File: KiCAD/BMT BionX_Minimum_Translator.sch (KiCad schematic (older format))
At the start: 18 parts

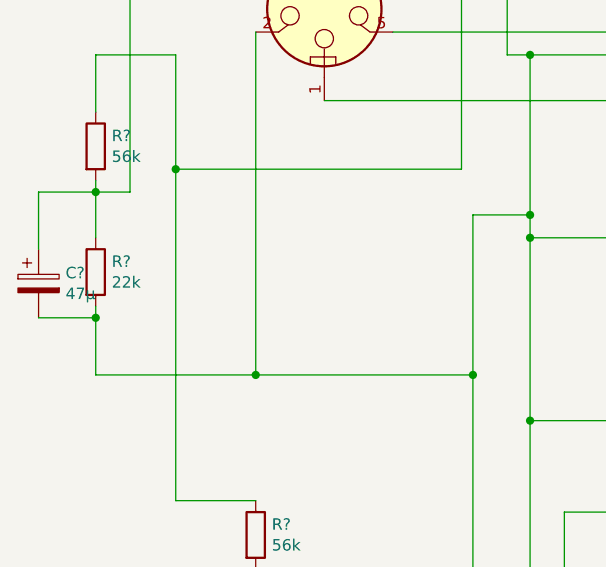
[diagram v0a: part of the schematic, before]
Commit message: Zener diode at HiSide-Switch input added
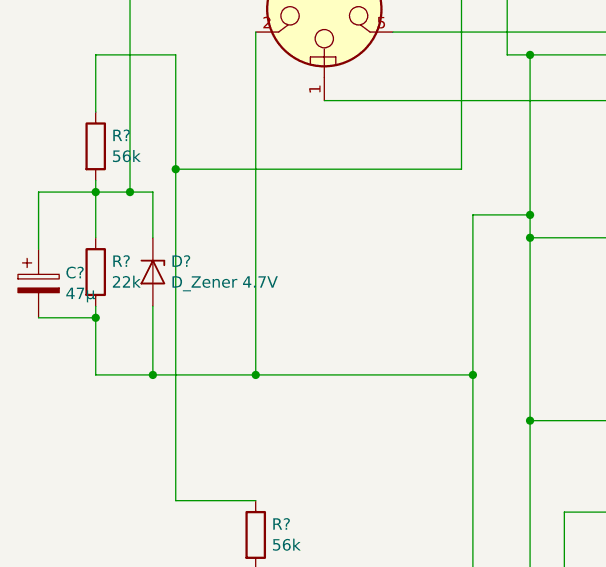
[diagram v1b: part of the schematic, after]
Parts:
- added D?: D_Zener 4.7V, symbol Device:D_Zener
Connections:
- wire segments 150 -> 154
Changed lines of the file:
@@
 	1250 4100 1250 4350
 Wire Wire Line
-	1250 4350 1950 4350
+	1250 4350 1500 4350
 Wire Wire Line
 	2200 2200 2200 1950
@@
 Wire Wire Line
 	3150 2950 4600 2950
+$Comp
+L Device:D_Zener D?
+U 1 1 5F25BD75
+P 1500 3900
+F 0 "D?" V 1454 3979 50  0000 L CNN
+F 1 "D_Zener 4.7V" V 1545 3979 50  0000 L CNN
+F 2 "" H 1500 3900 50  0001 C CNN
+F 3 "~" H 1500 3900 50  0001 C CNN
+	1    1500 3900
+	0    1    1    0
+$EndComp
+Wire Wire Line
+	1400 3550 1500 3550
+Wire Wire Line
+	1500 3550 1500 3750
+Connection ~ 1400 3550
+Wire Wire Line
+	1500 4050 1500 4350
+Connection ~ 1500 4350
+Wire Wire Line
+	1500 4350 1950 4350
 $EndSCHEMATC

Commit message: bugfix in pinout of BTS432
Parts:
- removed U?: BTS432, Package_TO_SOT_SMD:TO-263-7_TabPin4, symbol Power_Management:BTS50010-1TAD
- added U?: BTS432, Package_TO_SOT_SMD:TO-263-7_TabPin4, symbol Power_Management:BTS432
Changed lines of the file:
@@
 	1600 2950 1600 3450
 Connection ~ 1600 3450
-$Comp
-L Power_Management:BTS50010-1TAD U?
-U 1 1 5F329D26
-P 3050 2050
-F 0 "U?" H 3394 2096 50  0000 L CNN
-F 1 "BTS432" H 3394 2005 50  0000 L CNN
-F 2 "Package_TO_SOT_SMD:TO-263-7_TabPin4" H 3900 1750 50  0001 C CNN
-F 3 "https://www.infineon.com/dgdl/Infineon-BTS50010-1TAD-DS-v01_00-EN.pdf?fileId=5546d462576f34750157c38810ca55cd" H 3050 1650 50  0001 C CNN
-	1    3050 2050
-	1    0    0    -1
-$EndComp
 Connection ~ 1950 4350
 Wire Wire Line
@@
 Wire Wire Line
 	1500 4350 1950 4350
+$Comp
+L Power_Management:BTS432 U?
+U 1 1 5F27B110
+P 3050 2050
+F 0 "U?" H 3394 2096 50  0000 L CNN
+F 1 "BTS432" H 3394 2005 50  0000 L CNN
+F 2 "Package_TO_SOT_SMD:TO-263-7_TabPin4" H 3900 1750 50  0001 C CNN
+F 3 "https://www.infineon.com/dgdl/Infineon-BTS50010-1TAD-DS-v01_00-EN.pdf?fileId=5546d462576f34750157c38810ca55cd" H 3050 1650 50  0001 C CNN
+	1    3050 2050
+	1    0    0    -1
+$EndComp
 $EndSCHEMATC

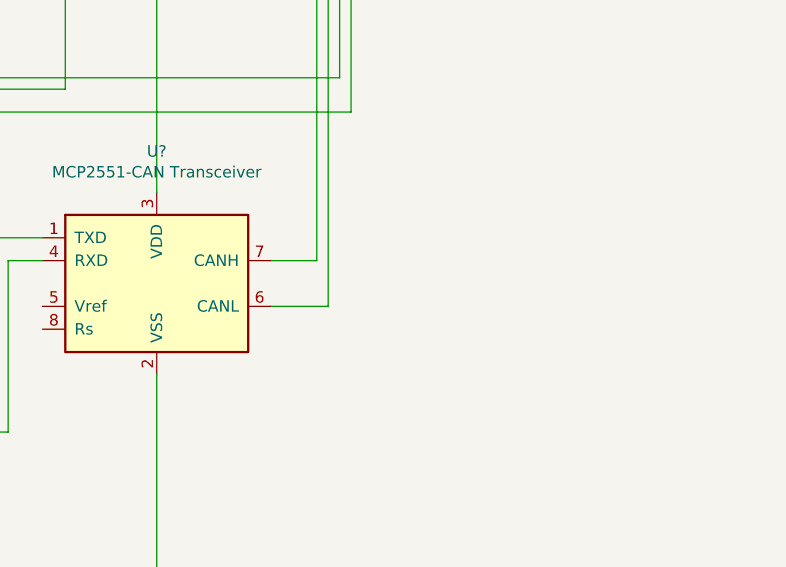
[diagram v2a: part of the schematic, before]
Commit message: Can termination resistor added
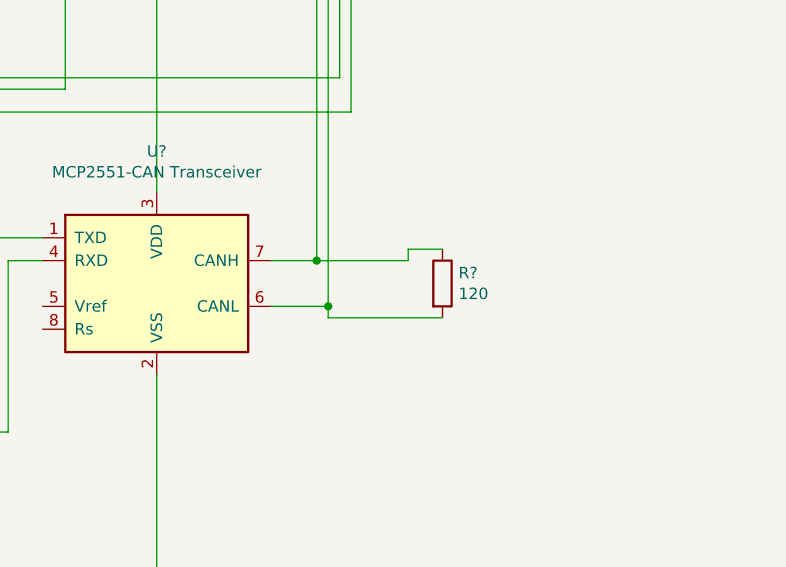
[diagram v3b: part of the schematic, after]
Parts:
- added R?: 120, symbol Device:R
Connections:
- net at J?.3 (Pin_3), U?.7 (CANH): now also R?.1
- net at J?.4 (Pin_4), U?.6 (CANL): now also R?.2
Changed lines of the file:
@@
 	1    0    0    -1
 $EndComp
+$Comp
+L Device:R R?
+U 1 1 5F28C11A
+P 7950 5650
+F 0 "R?" H 8020 5696 50  0000 L CNN
+F 1 "120" H 8020 5605 50  0000 L CNN
+F 2 "" V 7880 5650 50  0001 C CNN
+F 3 "~" H 7950 5650 50  0001 C CNN
+	1    7950 5650
+	1    0    0    -1
+$EndComp
+Wire Wire Line
+	7400 5550 7800 5550
+Wire Wire Line
+	7800 5550 7800 5500
+Wire Wire Line
+	7800 5500 7950 5500
+Connection ~ 7400 5550
+Wire Wire Line
+	7950 5800 7450 5800
+Wire Wire Line
+	7450 5800 7450 5750
+Connection ~ 7450 5750
 $EndSCHEMATC

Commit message: update KiCAD schematic
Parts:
- added J?: CAN Terminator, symbol Connector:Conn_01x02_Female
- added J?: CAN Connector, symbol Connector:Conn_01x02_Male
- added J?: Throttle connector, symbol Connector:Conn_01x03_Female
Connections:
- net at C?.2, D?.2 (A), J?.2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: now also J?.3 (Pin_3)
- net at J?.1 (Pin_1), U?.1 (OUT), U?.3 (VDD)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: now also J?.1 (Pin_1)
- net at J?.3 (Pin_3), U?.7 (CANH): now also J?.1 (Pin_1); no longer R?.1
- net at J?.4 (Pin_4), U?.6 (CANL): now also J?.2 (Pin_2); no longer R?.2
- net at U?.PA3: now also J?.2 (Pin_2)
- new net: J?.1 (Pin_1), R?.1
- new net: J?.2 (Pin_2), R?.2
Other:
- moved on the sheet: R?
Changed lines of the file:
@@
 Connection ~ 6700 2750
 Wire Wire Line
-	6700 2750 7550 2750
+	6700 2750 7300 2750
 Wire Wire Line
 	4850 7550 6700 7550
@@
 L Device:R R?
 U 1 1 5F28C11A
-P 7950 5650
-F 0 "R?" H 8020 5696 50  0000 L CNN
-F 1 "120" H 8020 5605 50  0000 L CNN
-F 2 "" V 7880 5650 50  0001 C CNN
-F 3 "~" H 7950 5650 50  0001 C CNN
-	1    7950 5650
-	1    0    0    -1
-$EndComp
-Wire Wire Line
-	7400 5550 7800 5550
-Wire Wire Line
-	7800 5550 7800 5500
-Wire Wire Line
-	7800 5500 7950 5500
+P 9400 5750
+F 0 "R?" H 9470 5796 50  0000 L CNN
+F 1 "120" H 9470 5705 50  0000 L CNN
+F 2 "" V 9330 5750 50  0001 C CNN
+F 3 "~" H 9400 5750 50  0001 C CNN
+	1    9400 5750
+	1    0    0    -1
+$EndComp
 Connection ~ 7400 5550
-Wire Wire Line
-	7950 5800 7450 5800
 Wire Wire Line
 	7450 5800 7450 5750
 Connection ~ 7450 5750
+$Comp
+L Connector:Conn_01x02_Female J?
+U 1 1 5F29F99C
+P 8700 5700
+F 0 "J?" H 8727 5676 50  0000 L CNN
+F 1 "CAN Terminator" H 8300 5850 50  0000 L CNN
+F 2 "" H 8700 5700 50  0001 C CNN
+F 3 "~" H 8700 5700 50  0001 C CNN
+	1    8700 5700
+	-1   0    0    -1
+$EndComp
+Wire Wire Line
+	8850 5700 8900 5700
+Wire Wire Line
+	9100 5700 9100 5600
+Wire Wire Line
+	9100 5600 9400 5600
+Wire Wire Line
+	8850 5800 8900 5800
+Wire Wire Line
+	9250 5800 9250 5900
+Wire Wire Line
+	9250 5900 9400 5900
+$Comp
+L Connector:Conn_01x02_Male J?
+U 1 1 5F2B86D5
+P 8350 5700
+F 0 "J?" H 8322 5674 50  0000 R CNN
+F 1 "CAN Connector" H 8650 5500 50  0000 R CNN
+F 2 "" H 8350 5700 50  0001 C CNN
+F 3 "~" H 8350 5700 50  0001 C CNN
+	1    8350 5700
+	-1   0    0    -1
+$EndComp
+Wire Wire Line
+	8150 5550 8150 5700
+Wire Wire Line
+	7450 5800 8150 5800
+Wire Wire Line
+	7400 5550 8150 5550
+Connection ~ 8900 5700
+Wire Wire Line
+	8900 5700 9100 5700
+Connection ~ 8900 5800
+Wire Wire Line
+	8900 5800 9250 5800
+$Comp
+L Connector:Conn_01x03_Female J?
+U 1 1 5F2F307C
+P 8150 3600
+F 0 "J?" H 8178 3626 50  0000 L CNN
+F 1 "Throttle connector" H 8178 3535 50  0000 L CNN
+F 2 "" H 8150 3600 50  0001 C CNN
+F 3 "~" H 8150 3600 50  0001 C CNN
+	1    8150 3600
+	1    0    0    -1
+$EndComp
+Wire Wire Line
+	7100 3150 7100 3700
+Wire Wire Line
+	7100 3700 7950 3700
+Connection ~ 7100 3150
+Wire Wire Line
+	7300 2750 7300 3500
+Wire Wire Line
+	7300 3500 7950 3500
+Connection ~ 7300 2750
+Wire Wire Line
+	7300 2750 7550 2750
+Wire Wire Line
+	7950 3600 7850 3600
+Wire Wire Line
+	7850 5000 3900 5000
+Wire Wire Line
+	3900 5000 3900 6000
+Wire Wire Line
+	3900 6000 3950 6000
+Wire Wire Line
+	7850 3600 7850 5000
 $EndSCHEMATC

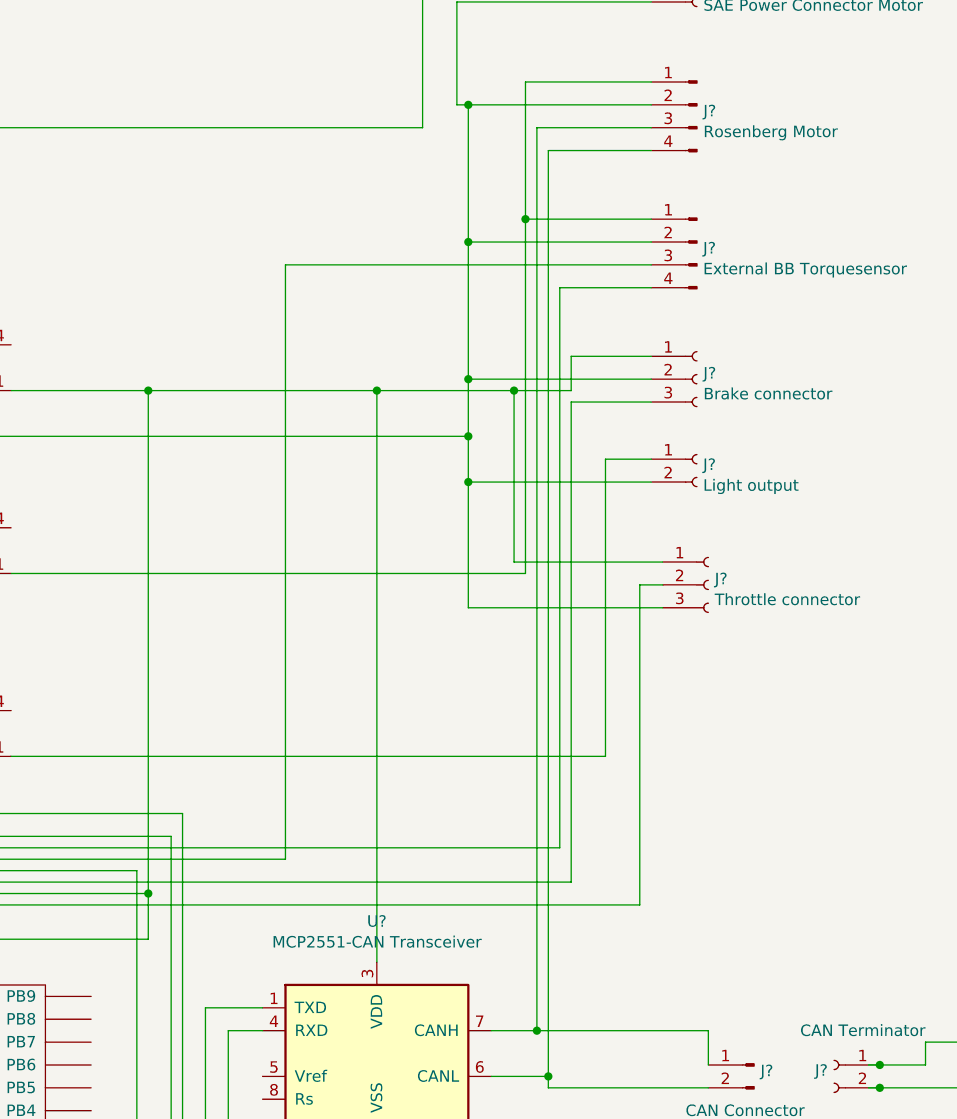
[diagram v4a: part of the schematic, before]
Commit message: voltage devider 5V -> 3.3v in schematic, adc-values print in debugmode
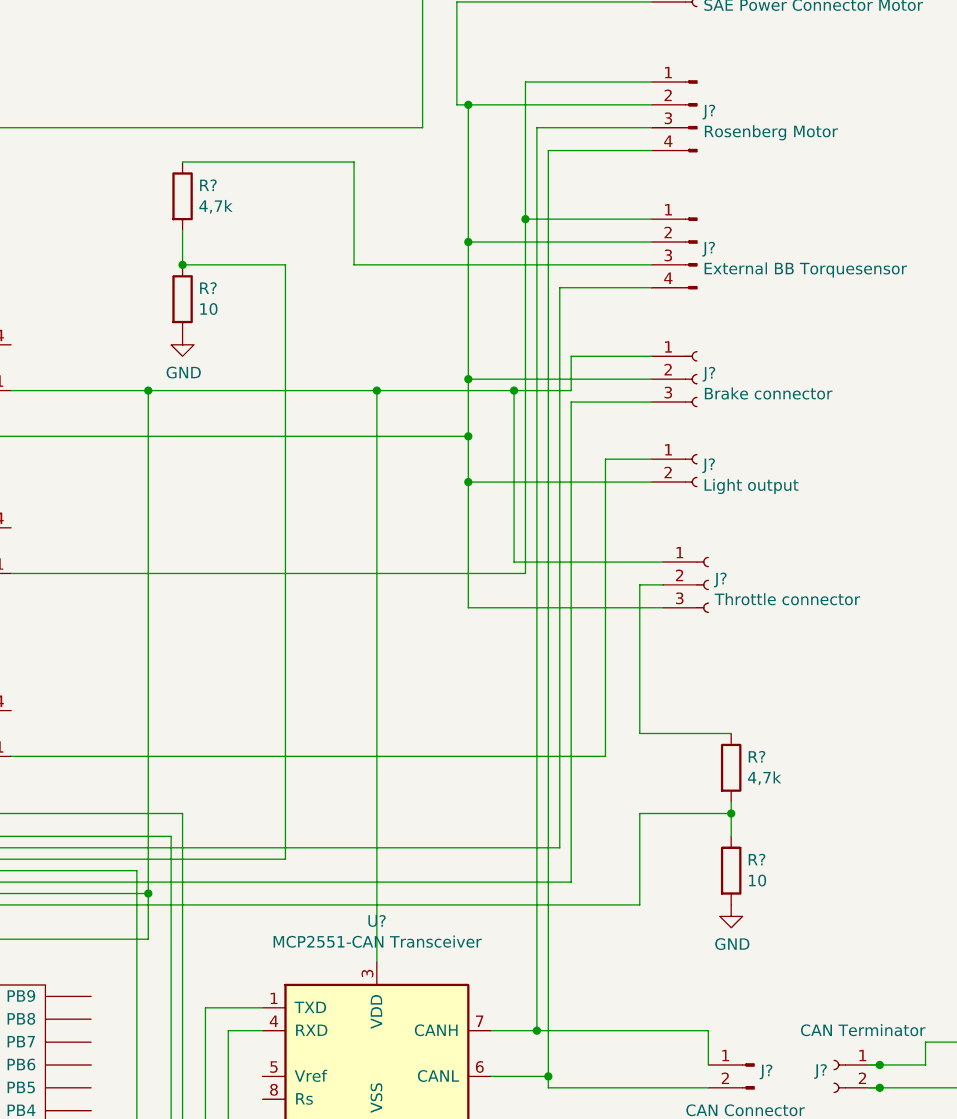
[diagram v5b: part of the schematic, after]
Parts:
- added R? (x2): 10, symbol Device:R
- added R? (x2): 4,7k, symbol Device:R
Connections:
- net GND: now also R?.2, R?.2
- net at J?.3 (Pin_3): now also R?.1; no longer U?.PA1
- net at U?.PA3: now also R?.1, R?.2; no longer J?.2 (Pin_2)
- new net: R?.1, R?.2, U?.PA1
- new net: J?.2 (Pin_2), R?.1
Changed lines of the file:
@@
 Connection ~ 3150 4550
 Wire Wire Line
-	7900 2200 6300 2200
+	7900 2200 6600 2200
 Wire Wire Line
 	6300 2200 6300 4800
@@
 	3900 6000 3950 6000
 Wire Wire Line
-	7850 3600 7850 5000
+	7850 3600 7850 4250
+$Comp
+L Device:R R?
+U 1 1 5F2CBEBF
+P 8250 4850
+F 0 "R?" H 8320 4896 50  0000 L CNN
+F 1 "10" H 8320 4805 50  0000 L CNN
+F 2 "" V 8180 4850 50  0001 C CNN
+F 3 "~" H 8250 4850 50  0001 C CNN
+	1    8250 4850
+	1    0    0    -1
+$EndComp
+$Comp
+L Device:R R?
+U 1 1 5F2CBEC5
+P 8250 4400
+F 0 "R?" H 8320 4446 50  0000 L CNN
+F 1 "4,7k" H 8320 4355 50  0000 L CNN
+F 2 "" V 8180 4400 50  0001 C CNN
+F 3 "~" H 8250 4400 50  0001 C CNN
+	1    8250 4400
+	1    0    0    -1
+$EndComp
+Wire Wire Line
+	8250 4550 8250 4600
+Wire Wire Line
+	7850 4250 8250 4250
+Wire Wire Line
+	7850 4600 8250 4600
+Wire Wire Line
+	7850 4600 7850 5000
+Connection ~ 8250 4600
+Wire Wire Line
+	8250 4600 8250 4700
+$Comp
+L power:GND #PWR?
+U 1 1 5F30BFB9
+P 8250 5000
+F 0 "#PWR?" H 8250 4750 50  0001 C CNN
+F 1 "GND" H 8255 4827 50  0000 C CNN
+F 2 "" H 8250 5000 50  0001 C CNN
+F 3 "" H 8250 5000 50  0001 C CNN
+	1    8250 5000
+	1    0    0    -1
+$EndComp
+$Comp
+L Device:R R?
+U 1 1 5F30EAB2
+P 5850 2350
+F 0 "R?" H 5920 2396 50  0000 L CNN
+F 1 "10" H 5920 2305 50  0000 L CNN
+F 2 "" V 5780 2350 50  0001 C CNN
+F 3 "~" H 5850 2350 50  0001 C CNN
+	1    5850 2350
+	1    0    0    -1
+$EndComp
+$Comp
+L Device:R R?
+U 1 1 5F30EAB8
+P 5850 1900
+F 0 "R?" H 5920 1946 50  0000 L CNN
+F 1 "4,7k" H 5920 1855 50  0000 L CNN
+F 2 "" V 5780 1900 50  0001 C CNN
+F 3 "~" H 5850 1900 50  0001 C CNN
+	1    5850 1900
+	1    0    0    -1
+$EndComp
+$Comp
+L power:GND #PWR?
+U 1 1 5F30EAC3
+P 5850 2500
+F 0 "#PWR?" H 5850 2250 50  0001 C CNN
+F 1 "GND" H 5855 2327 50  0000 C CNN
+F 2 "" H 5850 2500 50  0001 C CNN
+F 3 "" H 5850 2500 50  0001 C CNN
+	1    5850 2500
+	1    0    0    -1
+$EndComp
+Wire Wire Line
+	5850 2050 5850 2200
+Wire Wire Line
+	6600 2200 6600 1750
+Wire Wire Line
+	6600 1750 5850 1750
+Wire Wire Line
+	5850 2200 6300 2200
+Connection ~ 5850 2200
 $EndSCHEMATC

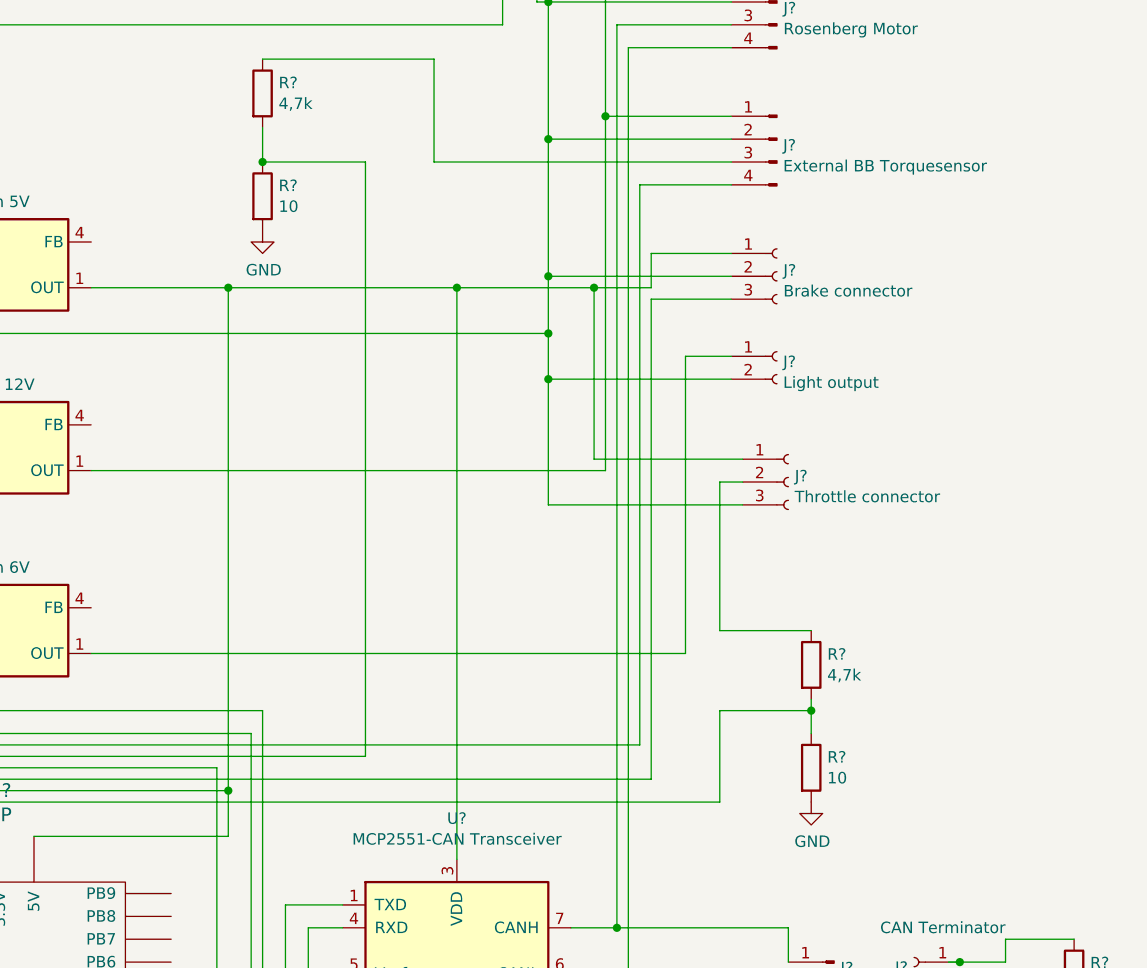
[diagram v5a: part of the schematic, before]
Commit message: capacitors on analog inputs added to schematic
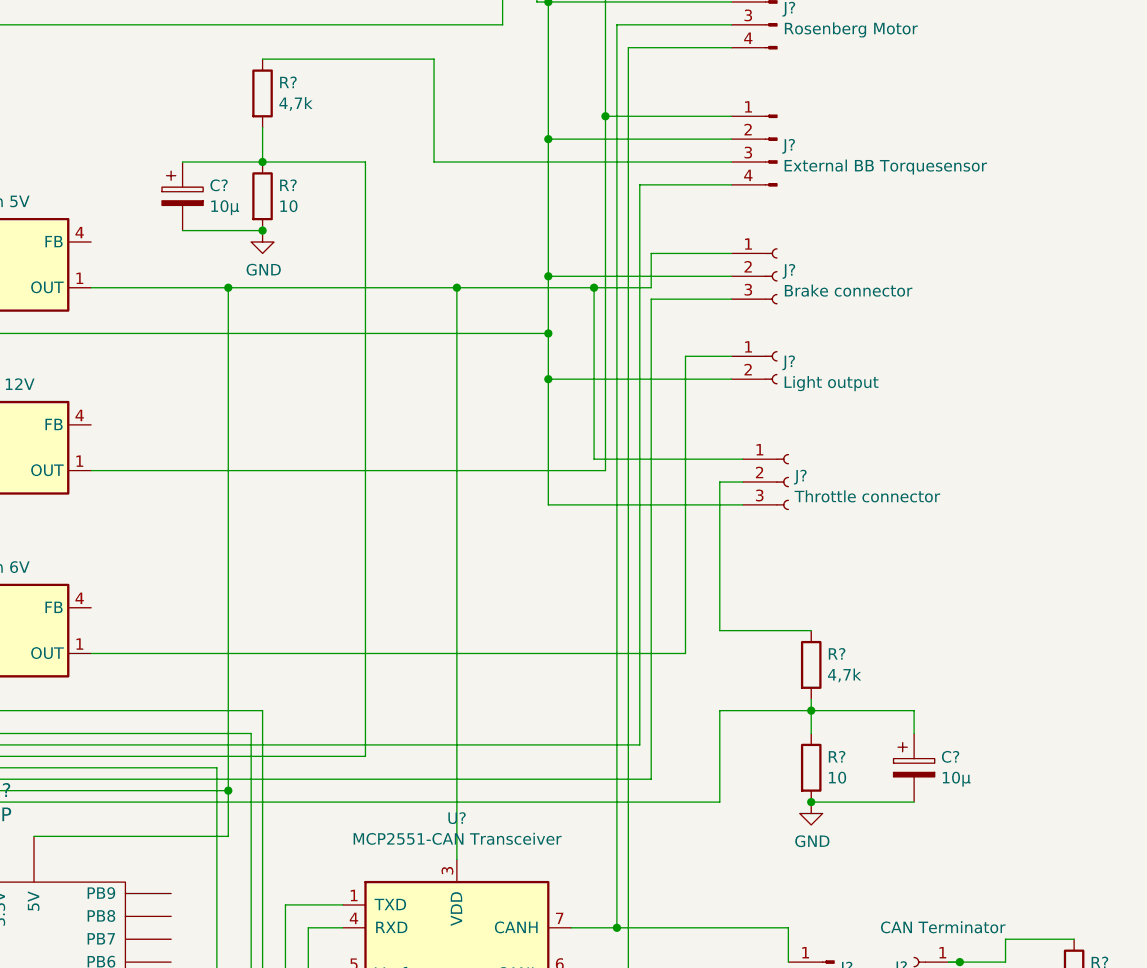
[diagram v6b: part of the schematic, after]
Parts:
- added C? (x2): 10µ, symbol Device:CP
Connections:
- net GND: now also C?.2, C?.2
- net at R?.1, R?.2, U?.PA1: now also C?.1
- net at R?.1, R?.2, U?.PA3: now also C?.1
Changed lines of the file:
@@
 	5850 2200 6300 2200
 Connection ~ 5850 2200
+$Comp
+L Device:CP C?
+U 1 1 5F2F700A
+P 8700 4850
+F 0 "C?" H 8818 4896 50  0000 L CNN
+F 1 "10µ" H 8818 4805 50  0000 L CNN
+F 2 "" H 8738 4700 50  0001 C CNN
+F 3 "~" H 8700 4850 50  0001 C CNN
+	1    8700 4850
+	1    0    0    -1
+$EndComp
+$Comp
+L Device:CP C?
+U 1 1 5F2F7EDF
+P 5500 2350
+F 0 "C?" H 5618 2396 50  0000 L CNN
+F 1 "10µ" H 5618 2305 50  0000 L CNN
+F 2 "" H 5538 2200 50  0001 C CNN
+F 3 "~" H 5500 2350 50  0001 C CNN
+	1    5500 2350
+	1    0    0    -1
+$EndComp
+Wire Wire Line
+	5500 2200 5850 2200
+Wire Wire Line
+	5500 2500 5850 2500
+Connection ~ 5850 2500
+Wire Wire Line
+	8700 4700 8700 4600
+Wire Wire Line
+	8700 4600 8250 4600
+Wire Wire Line
+	8700 5000 8250 5000
+Connection ~ 8250 5000
 $EndSCHEMATC
